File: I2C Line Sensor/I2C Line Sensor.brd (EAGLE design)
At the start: 63.5 x 12.1 mm, 33 parts, among them U1 ADS7830

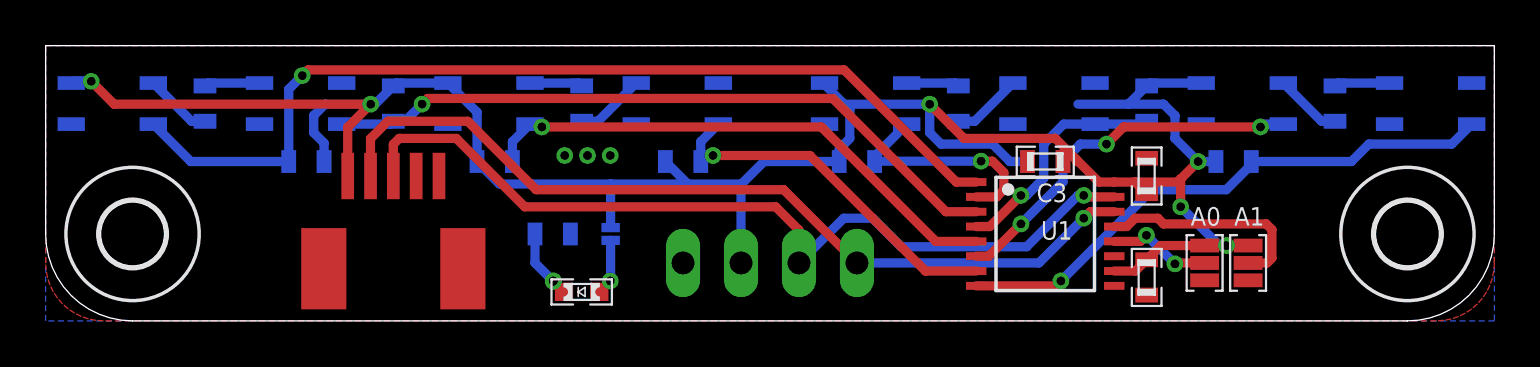
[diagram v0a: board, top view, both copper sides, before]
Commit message: CHanged mounting hole part
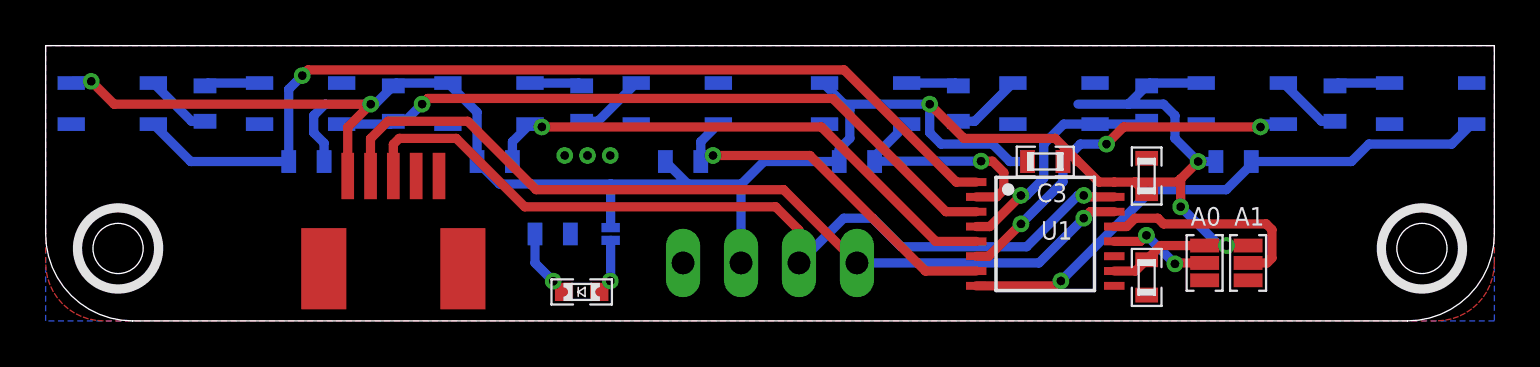
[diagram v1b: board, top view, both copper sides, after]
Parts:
- removed U$12, U$13: (no value), microbuilder:MOUNTINGHOLE_2.8
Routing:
- net N$11: track 3.08 -> 3.07 mm, vias 2 -> 1
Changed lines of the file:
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@@
 <?xml version="1.0" encoding="utf-8"?>
 <!DOCTYPE eagle SYSTEM "eagle.dtd">
-<eagle version="6.1">
+<eagle version="6.2">
 <drawing>
 <settings>
@@
 <layer number="50" name="dxf" color="7" fill="1" visible="no" active="yes"/>
 <layer number="51" name="tDocu" color="7" fill="1" visible="yes" active="yes"/>
-<layer number="52" name="bDocu" color="7" fill="1" visible="yes" active="yes"/>
+<layer number="52" name="bDocu" color="7" fill="1" visible="no" active="yes"/>
 <layer number="53" name="tGND_GNDA" color="7" fill="9" visible="no" active="no"/>
 <layer number="54" name="bGND_GNDA" color="1" fill="9" visible="no" active="no"/>
@@
 <text x="26.289" y="4.826" size="1.016" layer="52" ratio="12" rot="MR0">PWR On</text>
 <text x="21.336" y="2.54" size="1.6764" layer="51" ratio="12">PWR</text>
+<hole x="3.175" y="3.175" drill="2.2"/>
+<circle x="3.175" y="3.175" radius="1.778" width="0.4064" layer="21"/>
+<hole x="60.325" y="3.175" drill="2.2"/>
+<circle x="60.325" y="3.175" radius="1.778" width="0.4064" layer="21"/>
 </plain>
 <attributes>
@@
 <param name="mlMinCreamFrame" value="0mil"/>
 <param name="mlMaxCreamFrame" value="0mil"/>
-<param name="mlViaStopLimit" value="0mil"/>
+<param name="mlViaStopLimit" value="16mil"/>
 <param name="srRoundness" value="0"/>
 <param name="srMinRoundness" value="0mil"/>
@@
 <element name="U$7" library="SparkFun" package="QRE1113" value="QRE1113" x="52.451" y="9.525" smashed="yes" rot="MR180"/>
 <element name="U$8" library="SparkFun" package="QRE1113" value="QRE1113" x="60.706" y="9.525" smashed="yes" rot="MR180"/>
-<element name="U$12" library="microbuilder" package="MOUNTINGHOLE_2.8" value="" x="3.81" y="3.81" smashed="yes"/>
-<element name="U$13" library="microbuilder" package="MOUNTINGHOLE_2.8" value="" x="59.69" y="3.81" smashed="yes"/>
 <element name="U1" library="burr-brown" package="TSSOP16-PW" value="ADS7830" x="43.815" y="3.81" smashed="yes" rot="R270">
 <attribute name="NAME" x="43.628" y="3.56" size="0.8128" layer="25" ratio="12"/>
@@
 <contactref element="R13" pad="2"/>
 <wire x1="22.72" y1="1.27" x2="22.25" y2="1.74" width="0.4064" layer="1"/>
-<wire x1="22.25" y1="1.74" x2="22.25" y2="1.75" width="0.4064" layer="1"/>
-<via x="22.25" y="1.75" extent="1-16" drill="0.381"/>
 <via x="22.25" y="1.74" extent="1-16" drill="0.381"/>
 <wire x1="22.25" y1="1.74" x2="21.45" y2="2.54" width="0.4064" layer="16"/>
